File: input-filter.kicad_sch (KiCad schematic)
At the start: 28 parts

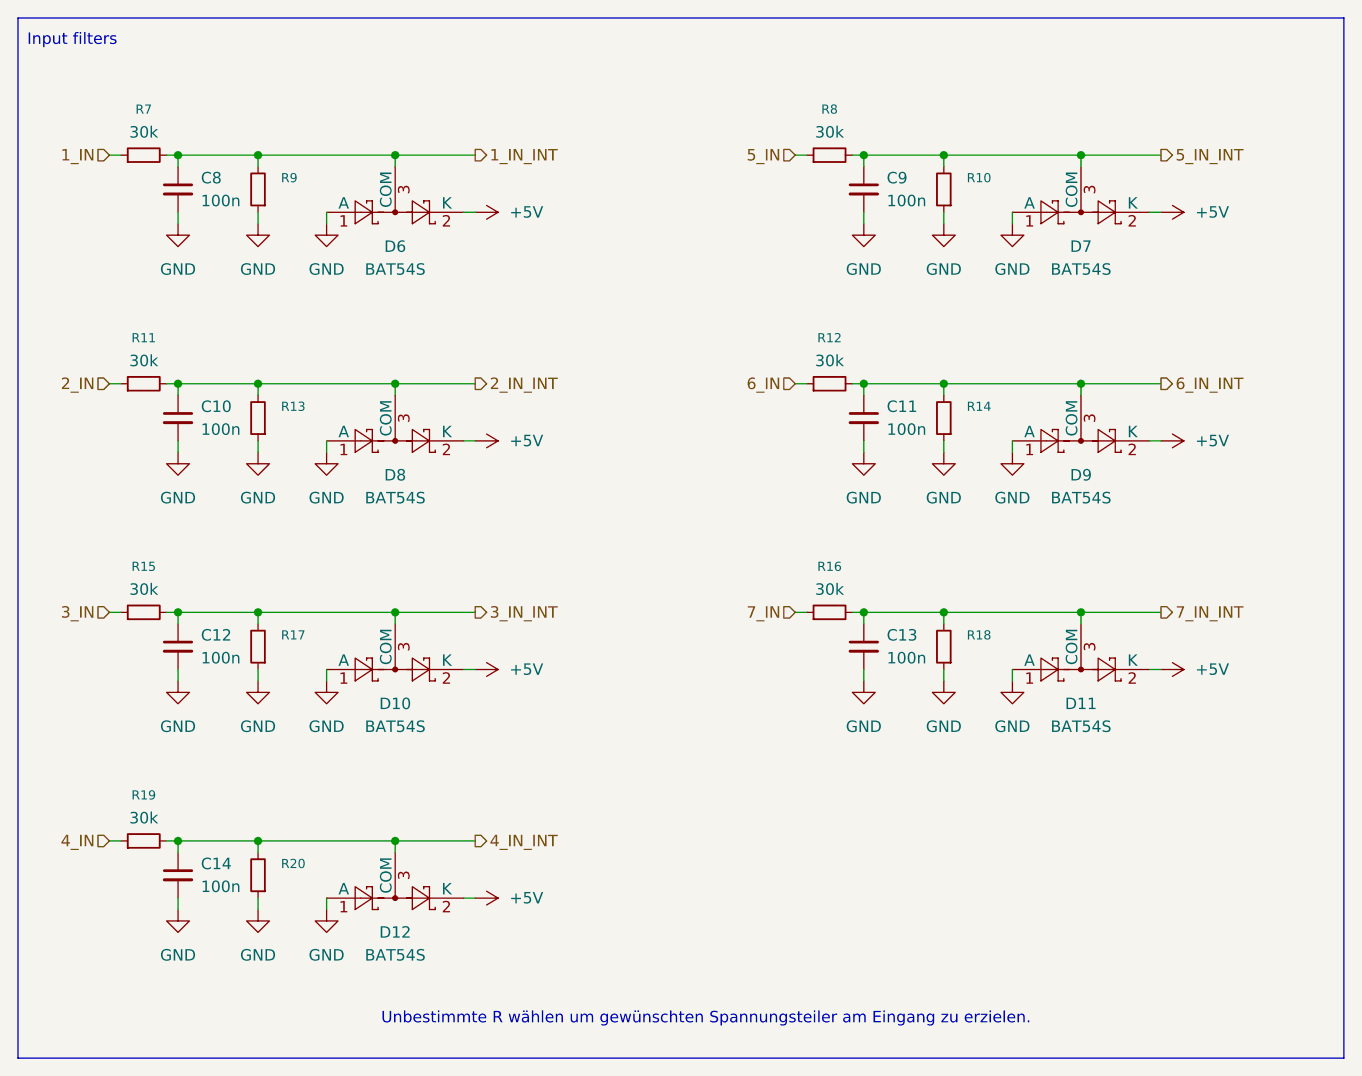
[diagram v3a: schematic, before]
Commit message: massive overhaul of pcb
* replace sub-d with 4x m12a 4pin circular connector
* fit board to bopla bolink case
* restructure entire board
* add second main voltage converter for powering input devices
* reduce inputs to 5
* remove 6 axis imu
* remove outputs
* remove mounting holes
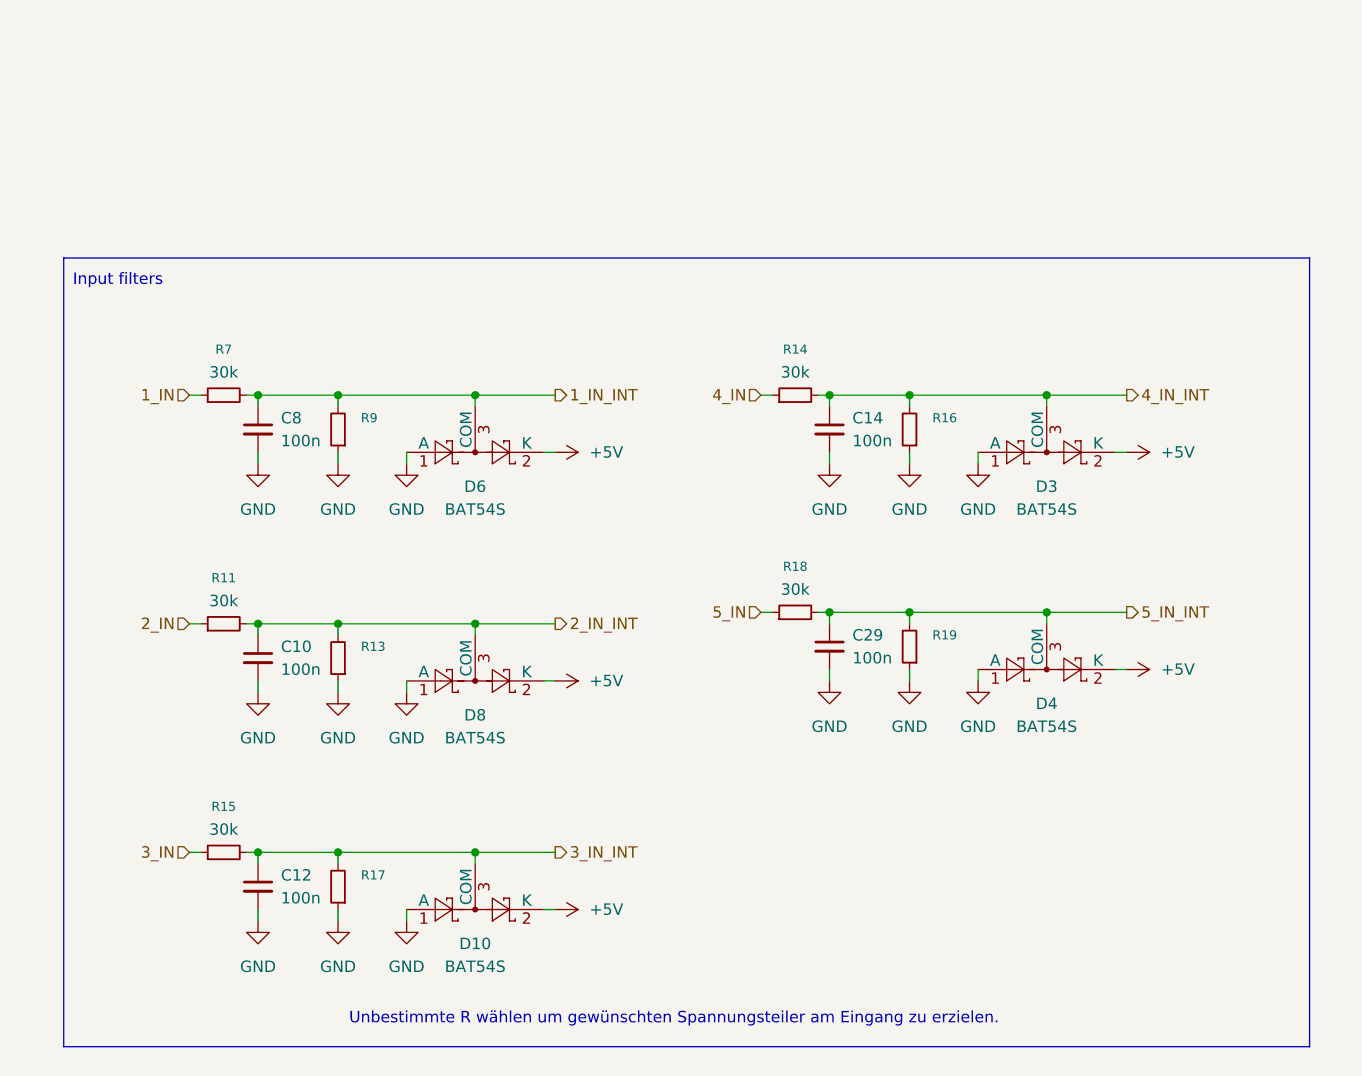
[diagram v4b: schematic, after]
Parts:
- removed C11, C13, C9: 100n, Capacitor_SMD:C_0603_1608Metric, symbol Device:C_Small
- removed D11, D12, D7, D9: BAT54S, Package_TO_SOT_SMD:SOT-23, symbol Diode:BAT54S
- removed R10, R20: ~, Resistor_SMD:R_0603_1608Metric, symbol Device:R_Small
- removed R12, R8: 30k, Resistor_SMD:R_0603_1608Metric, symbol Device:R_Small
- added C29: 100n, Capacitor_SMD:C_0603_1608Metric, symbol Device:C_Small
- added D3, D4: BAT54S, Package_TO_SOT_SMD:SOT-23, symbol Diode:BAT54S
- R14, R18: value ~ -> 30k
- R16, R19: value 30k -> ~
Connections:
- net 6_IN_INT is gone; now on net 4_IN_INT: R14.2
- net 7_IN is gone; now on net GND: R16.1
- net +5V: now also D3.2 (K), D4.2 (K)
- net 4_IN: now also R14.1; no longer R19.1
- net 4_IN_INT: now also R16.2, D3.3 (COM); no longer R19.2
- net 5_IN: now also R18.1
- net 5_IN_INT: now also R18.2, R19.2, C29.1, D4.3 (COM)
- net GND: now also R19.1, C29.2, D3.1 (A), D4.1 (A); no longer R14.1, R18.1
- removed net 7_IN_INT: R16.2, R18.2
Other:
- moved on the sheet: C10, C12, C8, D10, D6, D8, R11, R13, R15, R17, R7, R9

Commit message: update to kicad 10
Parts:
- R13, R16, R17, R19, R9: value ~ -> (none)

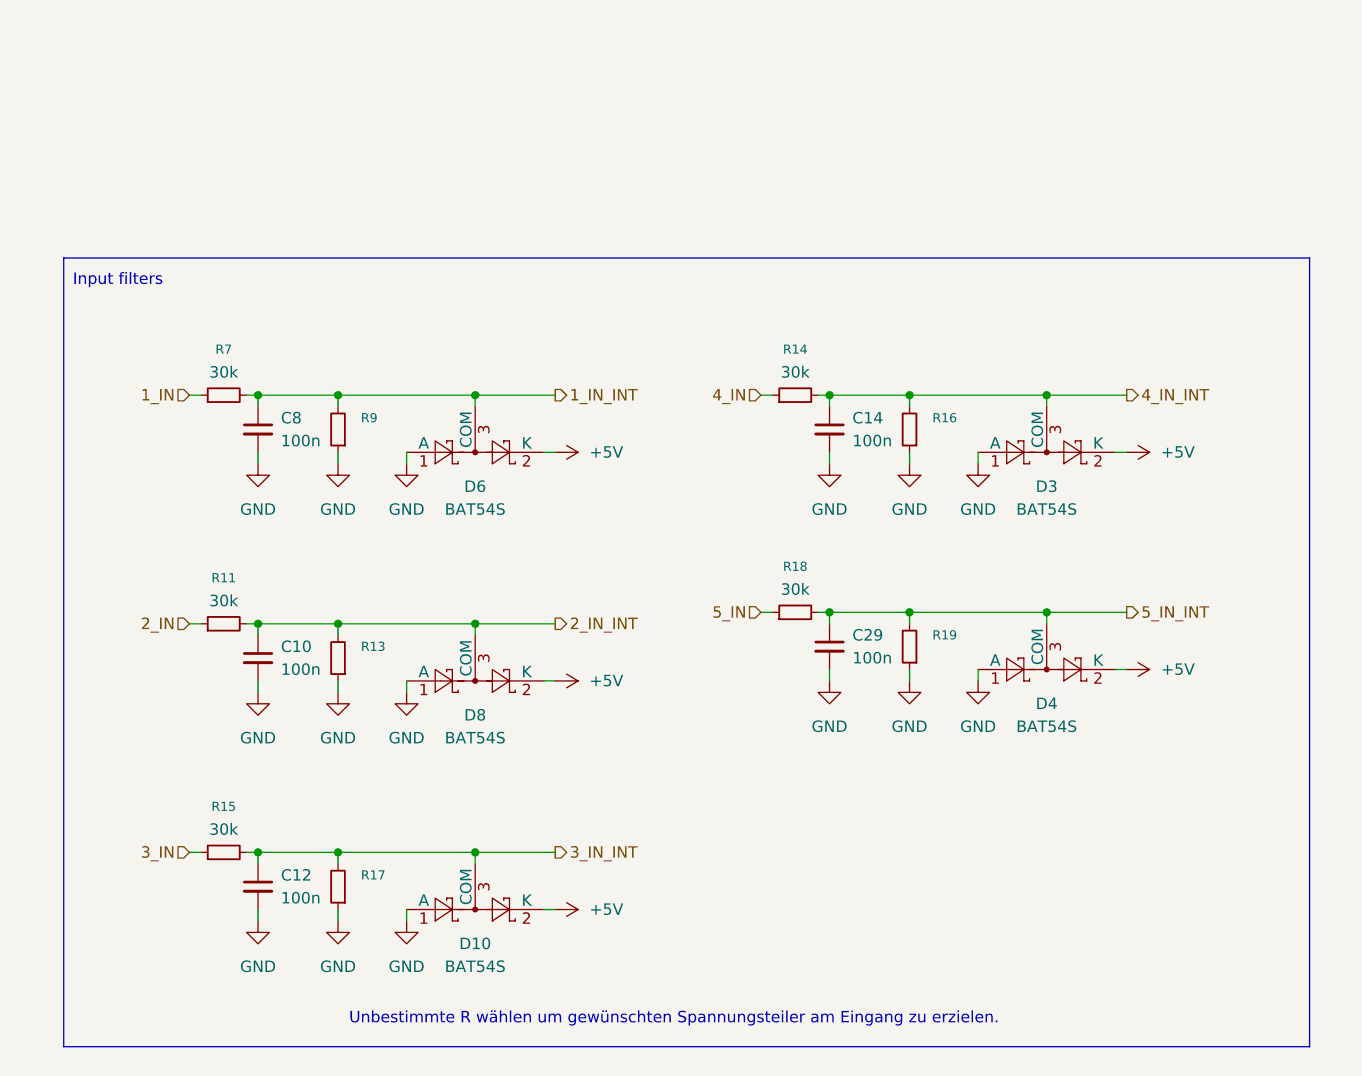
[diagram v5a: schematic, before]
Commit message: change esd protection to +3v3 reference voltage
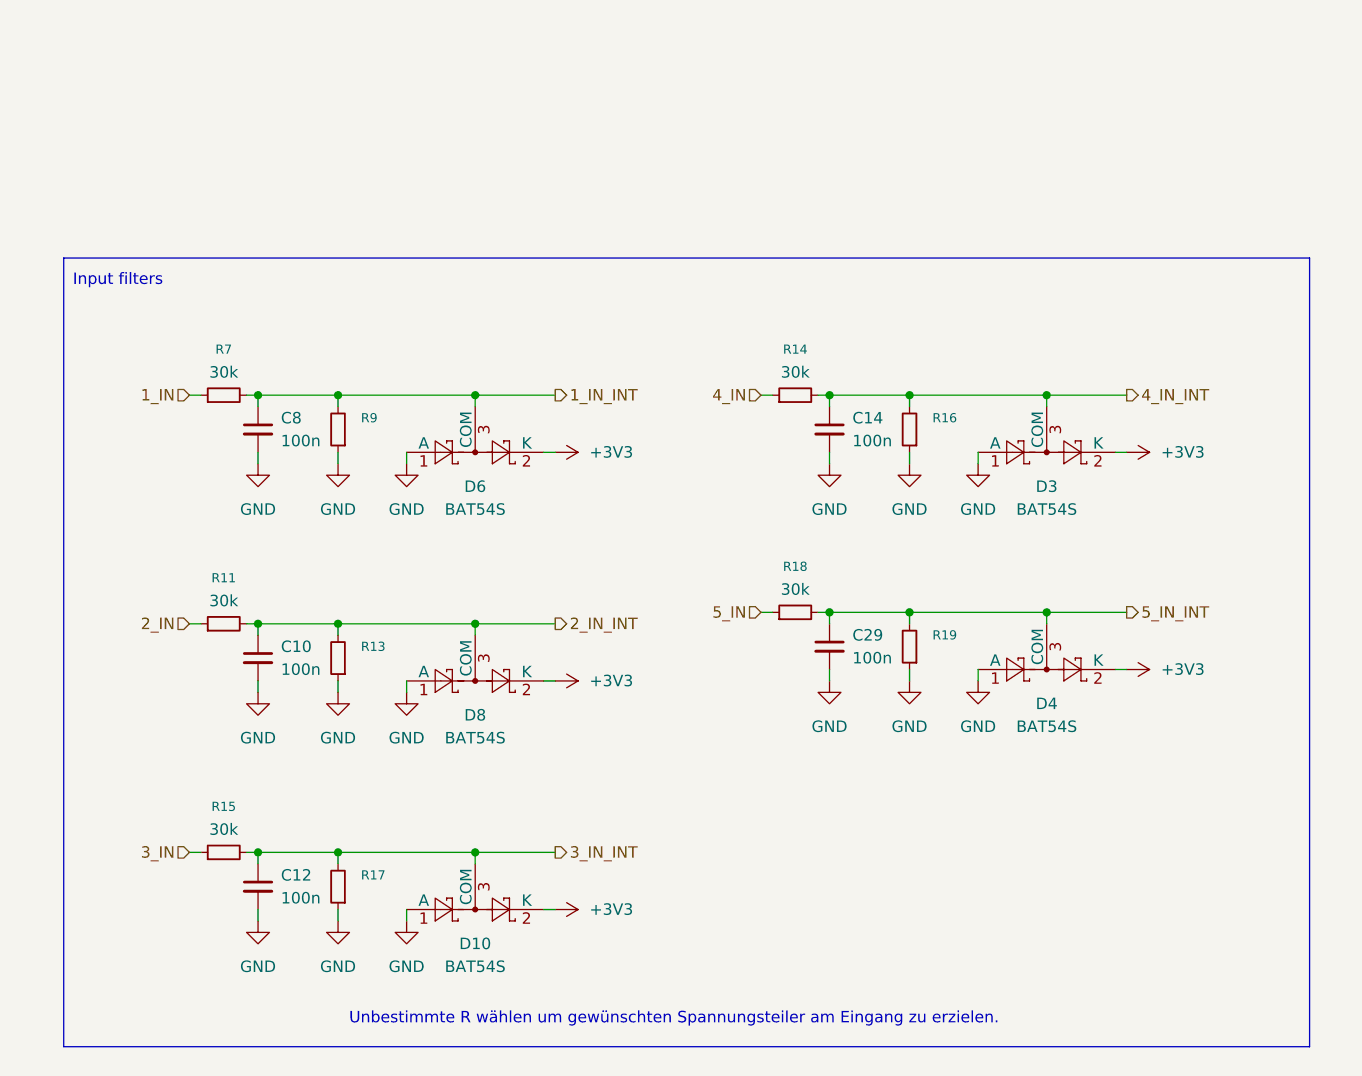
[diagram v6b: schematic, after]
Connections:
- net +5V renamed +3V3
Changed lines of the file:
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@@
 			)
 		)
-		(property "Value" "+5V"
+		(property "Value" "+3V3"
 			(at 138.43 134.6199 90)
 			(show_name no)
@@
 			)
 		)
-		(property "Value" "+5V"
+		(property "Value" "+3V3"
 			(at 138.43 83.8199 90)
 			(show_name no)
@@
 			)
 		)
-		(property "Value" "+5V"
+		(property "Value" "+3V3"
 			(at 201.93 107.9499 90)
 			(show_name no)
@@
 			)
 		)
-		(property "Value" "+5V"
+		(property "Value" "+3V3"
 			(at 138.43 109.2199 90)
 			(show_name no)
@@
 			)
 		)
-		(property "Value" "+5V"
+		(property "Value" "+3V3"
 			(at 201.93 83.8199 90)
 			(show_name no)
